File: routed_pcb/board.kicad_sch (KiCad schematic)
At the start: 25 parts

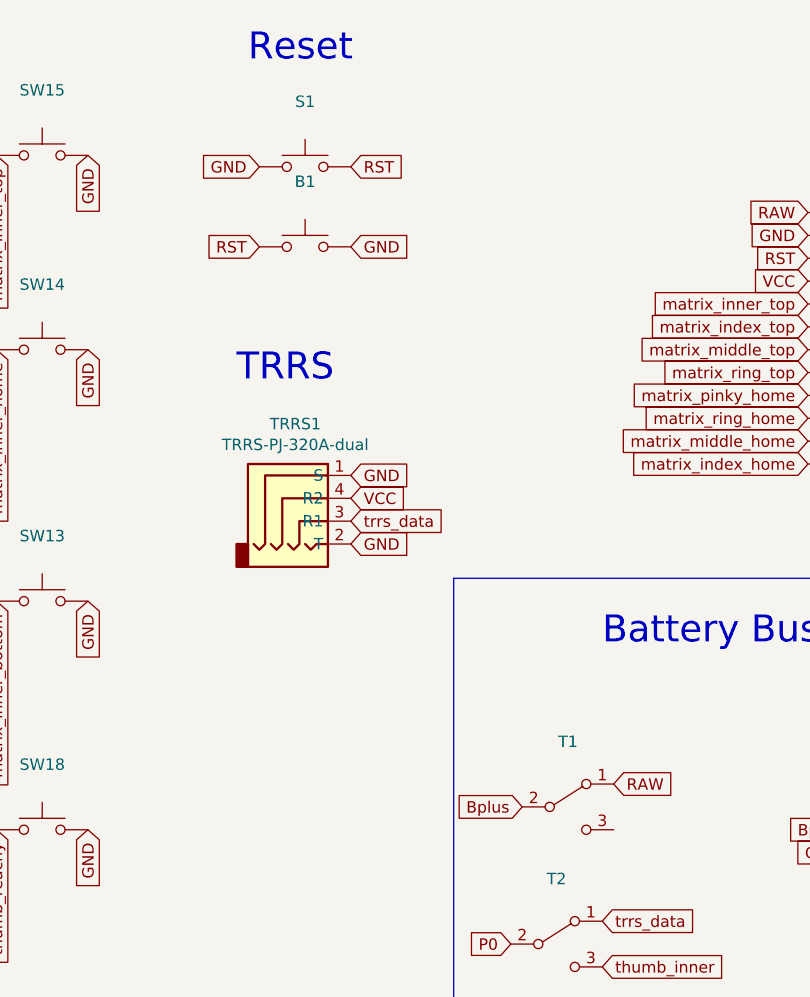
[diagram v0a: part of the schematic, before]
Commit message: update routed pcb to same as updated config
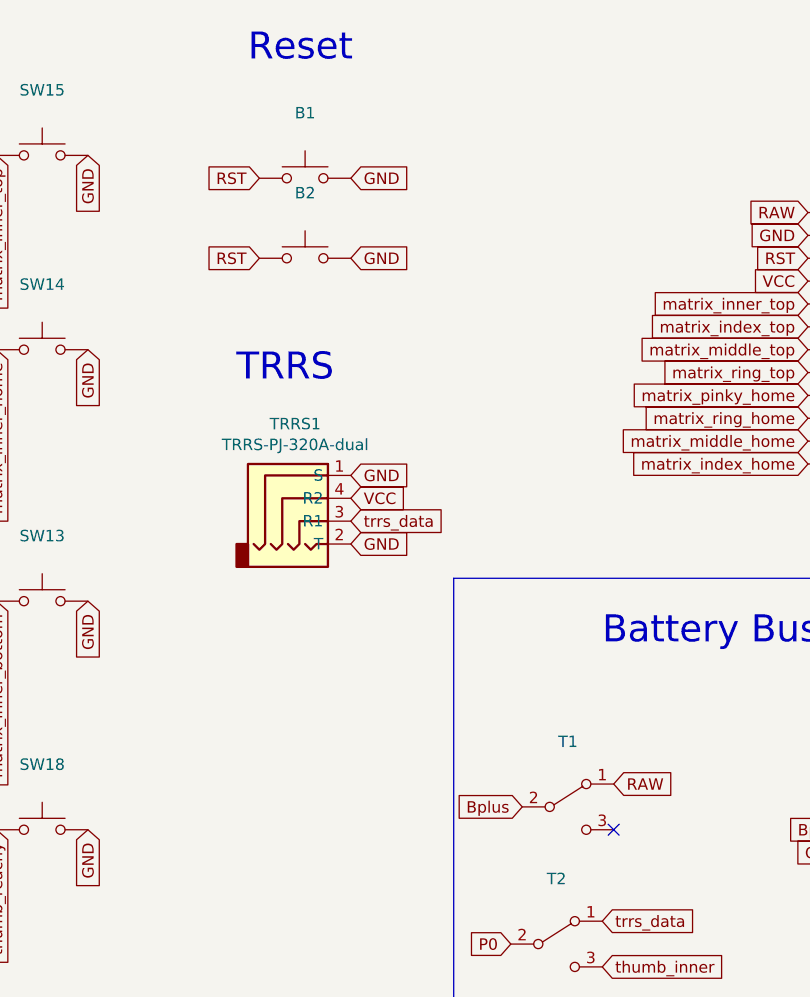
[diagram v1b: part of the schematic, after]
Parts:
- renumbered S1 to B2
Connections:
- net GND: now also B2.2; no longer B2.1
- net RST: now also B2.1; no longer B2.2
- no-connect marks 0 -> 1
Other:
- moved on the sheet: B1, B2
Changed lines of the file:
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@@
     (rev "0.1")
   )
+  (no_connect (at 156.21 104.14))
   (polyline (pts (xy 213.36 129.54) (xy 138.43 129.54))
     (stroke (width 0) (type default))
@@
     )
   )
+  (global_label "GND" (shape input) (at 127 40.64 0) (fields_autoplaced)
+    (effects (font (size 1.27 1.27)) (justify left))
+    (property "Intersheetrefs" "${INTERSHEET_REFS}" (at 133.8557 40.64 0)
+      (effects (font (size 1.27 1.27)) (justify left) hide)
+    )
+  )
   (global_label "GND" (shape input) (at 81.28 29.21 270) (fields_autoplaced)
     (effects (font (size 1.27 1.27)) (justify right))
@@
     )
   )
-  (global_label "GND" (shape input) (at 127 39.37 0) (fields_autoplaced)
-    (effects (font (size 1.27 1.27)) (justify left))
-    (property "Intersheetrefs" "${INTERSHEET_REFS}" (at 133.8557 39.37 0)
+  (global_label "GND" (shape input) (at 127 31.75 0) (fields_autoplaced)
+    (effects (font (size 1.27 1.27)) (justify left))
+    (property "Intersheetrefs" "${INTERSHEET_REFS}" (at 133.8557 31.75 0)
       (effects (font (size 1.27 1.27)) (justify left) hide)
     )
@@
     )
   )
-  (global_label "RST" (shape input) (at 127 30.48 0) (fields_autoplaced)
-    (effects (font (size 1.27 1.27)) (justify left))
-    (property "Intersheetrefs" "${INTERSHEET_REFS}" (at 133.4323 30.48 0)
-      (effects (font (size 1.27 1.27)) (justify left) hide)
-    )
-  )
   (global_label "matrix_index_bottom" (shape input) (at 71.12 78.74 270) (fields_autoplaced)
     (effects (font (size 1.27 1.27)) (justify right))
@@
     )
   )
+  (global_label "RST" (shape input) (at 116.84 40.64 180) (fields_autoplaced)
+    (effects (font (size 1.27 1.27)) (justify right))
+    (property "Intersheetrefs" "${INTERSHEET_REFS}" (at 111.0619 40.64 0)
+      (effects (font (size 1.27 1.27)) (justify right) hide)
+    )
+  )
   (global_label "matrix_ring_home" (shape input) (at 39.37 50.8 270) (fields_autoplaced)
     (effects (font (size 1.27 1.27)) (justify right))
@@
     )
   )
-  (global_label "RST" (shape input) (at 116.84 39.37 180) (fields_autoplaced)
-    (effects (font (size 1.27 1.27)) (justify right))
-    (property "Intersheetrefs" "${INTERSHEET_REFS}" (at 110.4077 39.37 0)
-      (effects (font (size 1.27 1.27)) (justify right) hide)
-    )
-  )
-  (global_label "GND" (shape input) (at 116.84 30.48 180) (fields_autoplaced)
-    (effects (font (size 1.27 1.27)) (justify right))
-    (property "Intersheetrefs" "${INTERSHEET_REFS}" (at 109.9843 30.48 0)
+  (global_label "RST" (shape input) (at 116.84 31.75 180) (fields_autoplaced)
+    (effects (font (size 1.27 1.27)) (justify right))
+    (property "Intersheetrefs" "${INTERSHEET_REFS}" (at 110.4077 31.75 0)
       (effects (font (size 1.27 1.27)) (justify right) hide)
     )
@@
     )
   )
-  (symbol (lib_id "Switch:SW_Push") (at 121.92 39.37 0) (unit 1)
-    (in_bom yes) (on_board yes) (dnp no)
-    (property "Reference" "B1" (at 121.92 32.131 0)
-      (effects (font (size 1.27 1.27)))
-    )
-    (property "Value" "~" (at 121.92 34.4424 0)
-      (effects (font (size 1.27 1.27)))
-    )
-    (property "Footprint" "kbd:ResetSW" (at 121.92 34.29 0)
-      (effects (font (size 1.27 1.27)) hide)
-    )
-    (property "Datasheet" "~" (at 121.92 34.29 0)
+  (symbol (lib_id "Switch:SW_Push") (at 121.92 31.75 0) (unit 1)
+    (in_bom yes) (on_board yes) (dnp no)
+    (property "Reference" "B1" (at 121.92 24.511 0)
+      (effects (font (size 1.27 1.27)))
+    )
+    (property "Value" "~" (at 121.92 26.8224 0)
+      (effects (font (size 1.27 1.27)))
+    )
+    (property "Footprint" "kbd:ResetSW" (at 121.92 26.67 0)
+      (effects (font (size 1.27 1.27)) hide)
+    )
+    (property "Datasheet" "~" (at 121.92 26.67 0)
       (effects (font (size 1.27 1.27)) hide)
     )
@@
     )
   )
-  (symbol (lib_id "Switch:SW_Push") (at 121.92 30.48 0) (unit 1)
-    (in_bom yes) (on_board yes) (dnp no)
-    (property "Reference" "S1" (at 121.92 23.241 0)
-      (effects (font (size 1.27 1.27)))
-    )
-    (property "Value" "~" (at 121.92 25.5524 0)
-      (effects (font (size 1.27 1.27)))
-    )
-    (property "Footprint" "Button_Switch_SMD:SW_SPST_B3U-1000P" (at 121.92 25.4 0)
-      (effects (font (size 1.27 1.27)) hide)
-    )
-    (property "Datasheet" "~" (at 121.92 25.4 0)
-      (effects (font (size 1.27 1.27)) hide)
-    )
-    (pin "1")
-    (pin "2")
-    (instances
-      (project "board"
-        (path "/42759be1-8852-47cd-90b4-32d161914658"
-          (reference "S1") (unit 1)
-        )
-      )
+  (symbol (lib_id "Switch:SW_Push") (at 121.92 40.64 0) (unit 1)
+    (in_bom yes) (on_board yes) (dnp no)
+    (property "Reference" "B2" (at 121.92 33.401 0)
+      (effects (font (size 1.27 1.27)))
+    )
+    (property "Value" "~" (at 121.92 35.7124 0)
+      (effects (font (size 1.27 1.27)))
+    )
+    (property "Footprint" "Button_Switch_SMD:SW_SPST_B3U-1000P" (at 121.92 35.56 0)
+      (effects (font (size 1.27 1.27)) hide)
+    )
+    (property "Datasheet" "~" (at 121.92 35.56 0)
+      (effects (font (size 1.27 1.27)) hide)
+    )
+    (pin "1")
+    (pin "2")
+    (instances
+      (project "board"
+        (path "/42759be1-8852-47cd-90b4-32d161914658"
+          (reference "B2") (unit 1)
+        )
+      )
